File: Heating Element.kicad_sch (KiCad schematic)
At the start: 20 parts, among them IC1 UCC23513QDWYRQ1, J1 Conn_01x04_Pin, U1 STP55NF06L, U2 MC7815CDTRKG

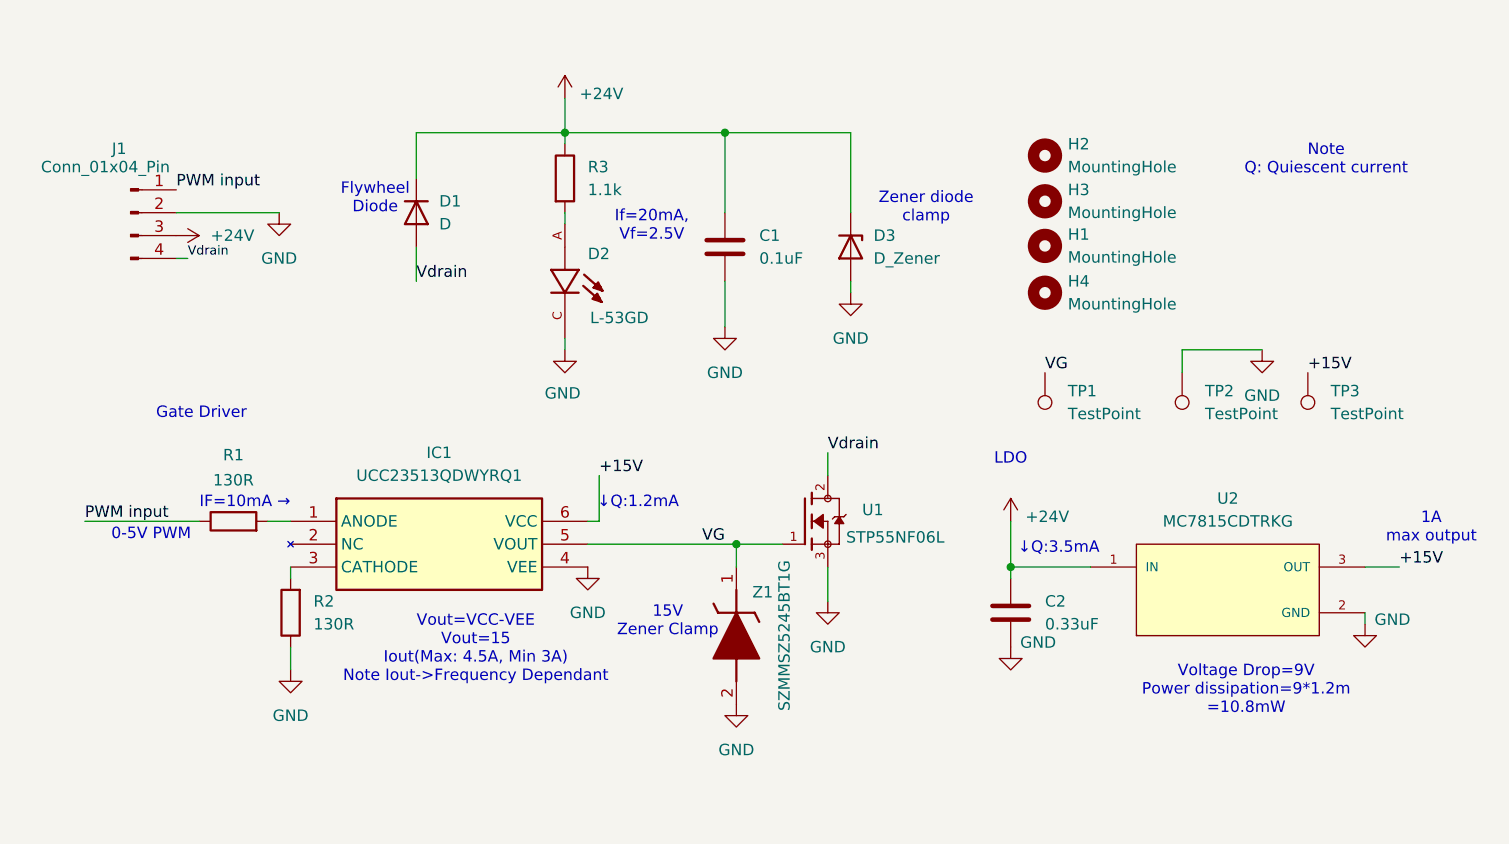
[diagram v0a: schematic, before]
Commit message: Updated schematic and PCB
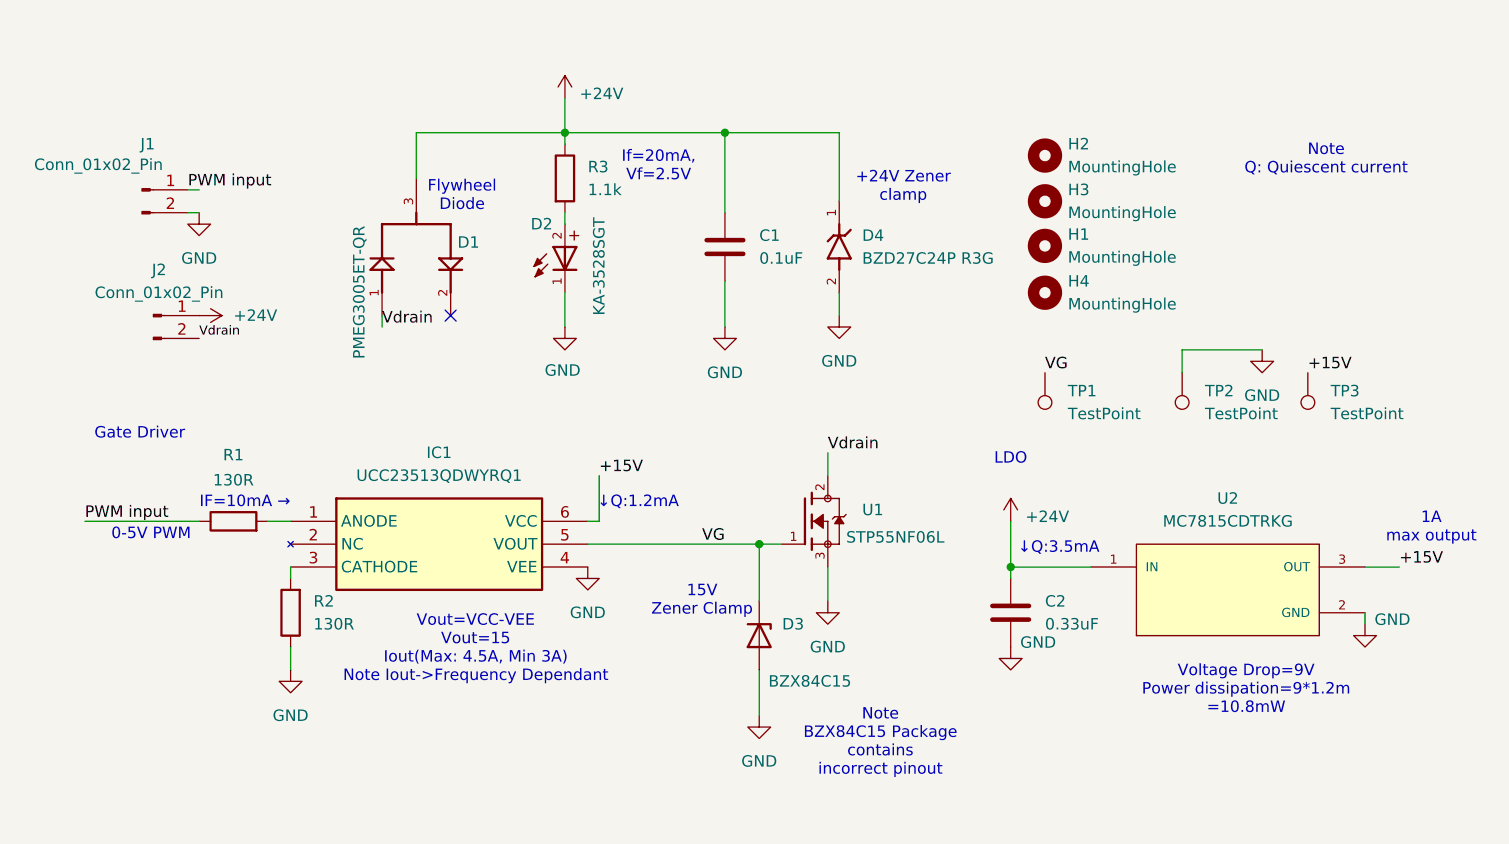
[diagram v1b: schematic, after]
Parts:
- removed D1: D, Diode_THT:D_DO-201AD_P15.24mm_Horizontal, symbol Device:D
- removed D2: L-53GD, L-53GD:LEDRD254W50D500H1060, symbol L-53GD:L-53GD
- removed D3: D_Zener, Diode_THT:D_DO-15_P15.24mm_Horizontal, symbol Device:D_Zener
- removed J1: Conn_01x04_Pin, Connector:NS-Tech_Grove_1x04_P2mm_Vertical, symbol Connector:Conn_01x04_Pin
- removed Z1: SZMMSZ5245BT1G, SZMMSZ5245BT1G_Kicad:SOD3716X135N, symbol SZMMSZ5245BT1G:SZMMSZ5245BT1G
- added D1: PMEG3005ET-QR, BAS70-7:SOT23, symbol BAS70-7:BAS70-7
- added D2: KA-3528SGT, WL-SMTW_3528:WL-SMTW_3528, symbol WL-SMTW_3528:WL-SMTW_3528
- added D3: BZX84C15, Package_TO_SOT_SMD:SOT-23, symbol Diode:BZX84Cxx
- added D4: BZD27C24P R3G, BZD27C10P:SODFL3618X143N, symbol BZD27C10P:BZD27C10P
- added J1, J2: Conn_01x02_Pin, Connector_PinSocket_2.00mm:PinSocket_1x02_P2.00mm_Vertical, symbol Connector:Conn_01x02_Pin
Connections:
- net +24V: now also D1.3, D4.1, J2.1 (Pin_1)
- net GND: now also D2.1, D3.1 (A), D4.2, J1.2 (Pin_2)
- net PWM input: now also J1.1 (Pin_1)
- net VG: now also D3.3 (K)
- net Vdrain: now also D1.1, J2.2 (Pin_2)
- net at R3.2: now also D2.2
- no-connect marks 0 -> 1
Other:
- note added: "+24V Zener clamp"
- note added: "Note BZX84C15 Package contains incorrect pinout"
- note removed: "Zener diode clamp"

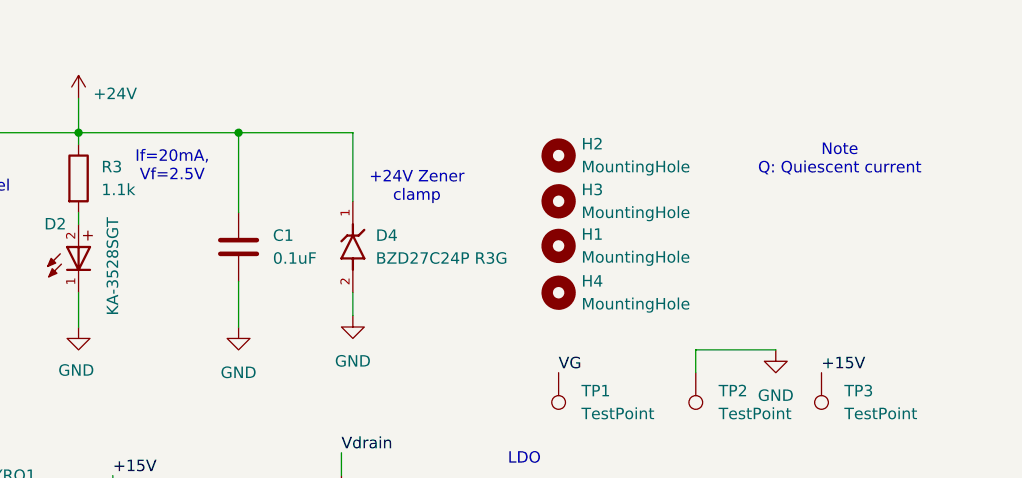
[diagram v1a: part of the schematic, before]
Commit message: Updated Schematic components (all smd) Updated PCB layout (includes schematic changes and routing) Updtaed Gerber files
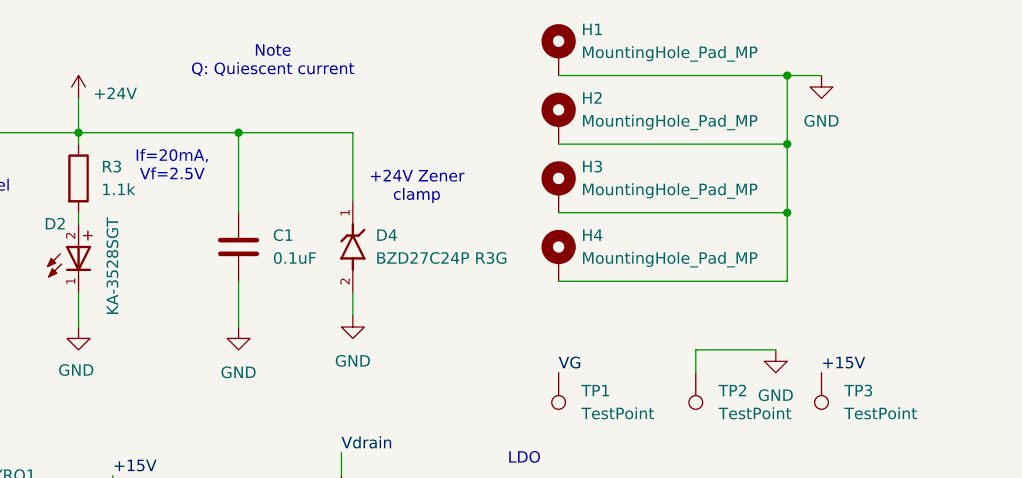
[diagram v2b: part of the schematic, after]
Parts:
- removed H1, H2, H3, H4: MountingHole, MountingHole:MountingHole_2.2mm_M2, symbol Mechanical:MountingHole
- added H1, H2, H3, H4: MountingHole_Pad_MP, MountingHole:MountingHole_2.2mm_M2_DIN965_Pad, symbol Mechanical:MountingHole_Pad_MP
- C1, C2: Tolerance (none) -> ±10%; Voltage (none) -> 50V dc
- D1: Availability In Stock -> (none); Check_prices https://www.snapeda.com/parts/BAS70-7/Diodes+Inc./view-part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 -> (none); Description_1 Diode Schottky 70V 0.07A 3-Pin SOT-23 T/R Diode Schottky 70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 -> (none); MF NEXPERIA -> (none); MFR (none) -> NEXPERIA; MP BAS70-7 -> (none); Package SOT-23 Diodes Inc. -> (none); Price None -> (none); SnapEDA_Link https://www.snapeda.com/parts/BAS70-7/Diodes+Inc./view-part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 -> (none)
- D2: Availability In Stock -> (none); Check_prices https://www.snapeda.com/parts/150141VS73100/Wurth+Electroni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 -> (none); MP 150141VS73100 -> (none); Price None -> (none); SnapEDA_Link https://www.snapeda.com/parts/150141VS73100/Wurth+Electroni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 -> (none)
- D3: Package (none) -> SOT-23
- D4: Availability In Stock -> (none); Check_prices https://www.snapeda.com/parts/BZD27C10P/Taiwan+Semiconducto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 -> (none); Description_1 Sub SMA, 1000mW, 6%, Zener Diode -> (none); MANUFACTURER Taiwan Semiconductor -> (none); MAXIMUM_PACKAGE_HEIGHT 1.43mm -> (none); MF Taiwan Semiconductor -> (none); MP BZD27C10P -> (none); PARTREV AB2103 -> (none); Price None -> (none); STANDARD IPC-7351B -> (none); SnapEDA_Link https://www.snapeda.com/parts/BZD27C10P/Taiwan+Semiconducto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 -> (none)
- J2, TP1, TP2, TP3: now left out of the parts list
- R1, R2: Tolerance (none) -> ±1%
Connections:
- net GND: now also H1.MP, H2.MP, H3.MP, H4.MP

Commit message: updated Heating PCB
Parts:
- removed J1: Conn_01x02_Pin, Connector_PinSocket_2.00mm:PinSocket_1x02_P2.00mm_Vertical, symbol Connector:Conn_01x02_Pin
- added J1: Conn_01x04_Pin, Connector_PinSocket_2.54mm:PinSocket_1x04_P2.54mm_Vertical, symbol Connector:Conn_01x04_Pin
- added R3: 2.4k, Resistor_SMD:R_1206_3216Metric, symbol Device:R
- added R5: 15k, Resistor_SMD:R_1206_3216Metric, symbol Device:R
- added R6: 1.1k, Resistor_SMD:R_1206_3216Metric, symbol Device:R
- J2: footprint Connector_PinSocket_2.00mm:PinSocket_1x02_P2.00mm_Vertical -> Connector_PinHeader_2.54mm:PinHeader_1x02_P2.54mm_Vertical
- renumbered TP3 to +15V_TP1, TP2 to GND_TP1, R3 to R4, TP1 to VG_TP1
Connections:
- net +24V: now also J1.3 (Pin_3), R3.1, R6.1; no longer D1.3, D4.1
- net GND: now also J1.2 (Pin_2), J1.4 (Pin_4)
- net PWM input: now also J1.1 (Pin_1)
- net VG: now also R5.1; no longer D3.3 (K)
- new net: D4.1, R6.2
- new net: D1.3, R3.2
- new net: D3.3 (K), R5.2
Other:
- note added: "10mA↓"
- note added: "15V"
- note added: "22mA↓"
- note added: "INPUT"
- note added: "OUTPUT"
- note added: "Ptot=1W"
- note added: "Ptot=1W Zener Impedance@25mA= 15ohm"
- note added: "↓1mA"
- moved on the sheet: D1, D3, H1, H2, H3, H4, J2, U1
